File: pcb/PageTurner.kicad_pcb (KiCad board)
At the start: 2 copper layers, 32 x 20 mm, 21 parts, among them J1 AudioJack2, J2 AudioJack2, J3 USB_C_Receptacle, J5 TC2030_SWD, SW1 RST, SW2 BOOT, U1 STM32F042F6Px, U2 TPS7A0533PDBV

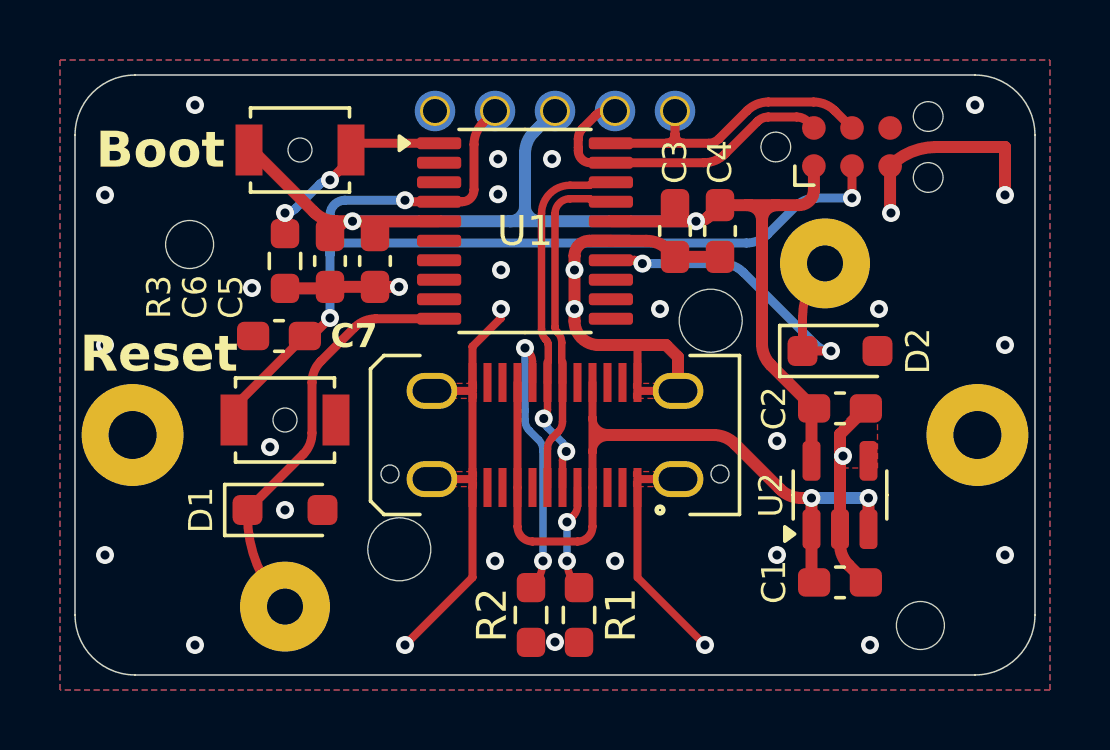
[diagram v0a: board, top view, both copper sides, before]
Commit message: Switch to a cheaper and smaller USB connector
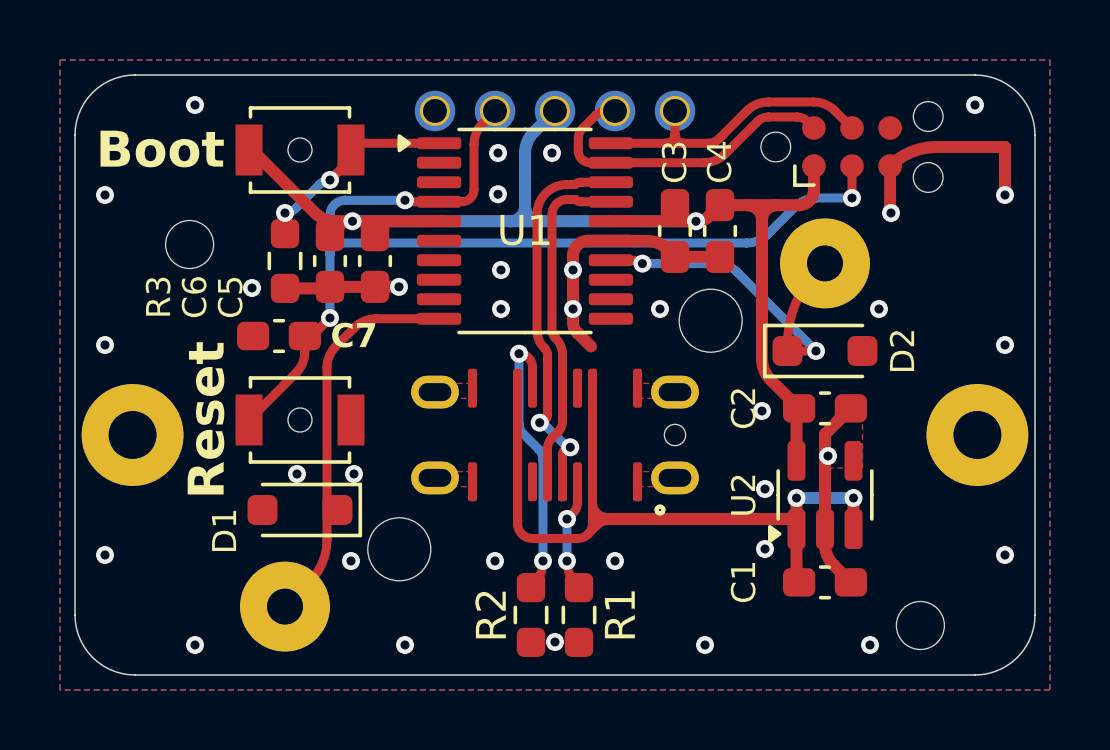
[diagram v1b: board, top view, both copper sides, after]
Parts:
- J3: footprint PageTurner:USB_C_Receptacle_JAE_DX07S024WJ3R400 -> PageTurner:USB_C_Receptacle_GCT_USB_4145
- moved C1 0.50 mm to (109.0, 104.9)
- moved C2 0.50 mm to (109.0, 99.1)
- moved D1 0.50 mm to (91.5, 102.5), turned to 180 degrees
- moved D2 0.50 mm to (109.0, 97.2)
- moved SW1 0.50 mm to (91.5, 99.5)
- moved U2 0.50 mm to (109.0, 102.0)
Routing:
- net GND: track 55.1 -> 25.7 mm, vias 32 -> 34
- net D+: track 11.8 -> 12.8 mm
- net VBUS: track 27.8 -> 26.9 mm
- net SW1: track 13.9 -> 13.0 mm

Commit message: Switch to 4 layers, add USB ESD diode
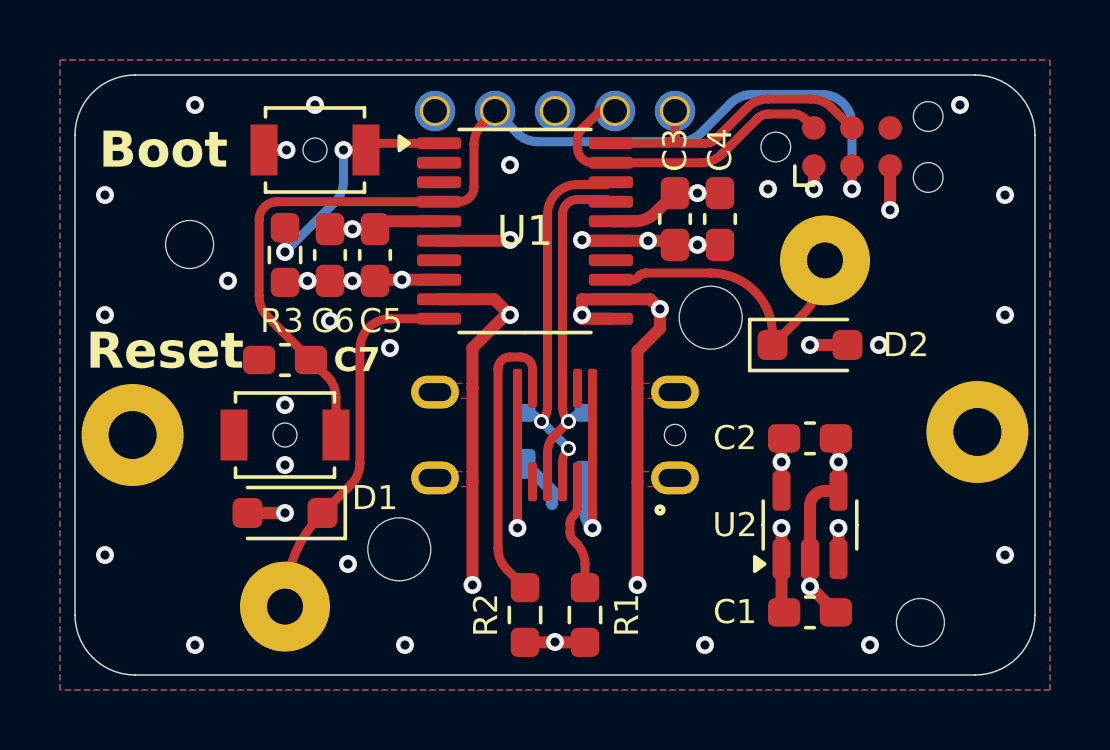
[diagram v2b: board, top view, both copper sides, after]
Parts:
- added D3: PRTR5V0U2X, Package_TO_SOT_SMD:SOT-143, B.Cu at (100.0, 100.2)
- moved C1 1.12 mm to (108.5, 105.9)
- moved C2 1.12 mm to (108.5, 100.1)
- moved U2 1.12 mm to (108.5, 103.0)
- moved C7 0.82 mm to (91.0, 97.5)
- moved SW1 0.71 mm to (91.0, 100.0), turned to 180 degrees
- moved D2 0.54 mm to (108.5, 97.0)
- moved D1 0.51 mm to (91.0, 102.6)
- moved SW2 0.50 mm to (92.0, 90.5)
- moved C3 0.40 mm to (104.0, 92.8)
- moved C4 0.40 mm to (105.5, 92.8)
- moved C5 0.20 mm to (94.0, 94.0)
- moved C6 0.20 mm to (92.5, 94.0)
- moved R1 0.20 mm to (101.0, 106.0)
- moved R2 0.20 mm to (99.0, 106.0)
- moved R3 0.20 mm to (91.0, 94.0)
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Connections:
- U1 pad 11: unconnected-(U1-PA5-Pad11) -> GND
- U1 pad 12: unconnected-(U1-PA6-Pad12) -> GND
- U1 pad 13: unconnected-(U1-PA7-Pad13) -> SW2
- U1 pad 14: SW2 -> unconnected-(U1-PB1-Pad14)
- U1 pad 6: unconnected-(U1-PA0-Pad6) -> GND
- U1 pad 7: unconnected-(U1-PA1-Pad7) -> GND
- U1 pad 8: unconnected-(U1-PA2-Pad8) -> GND
- U1 pad 9: unconnected-(U1-PA3-Pad9) -> GND
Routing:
- net +3V3: track 43.1 -> 10.6 mm, vias 2 -> 5
- net GND: track 25.7 -> 52.5 mm, vias 34 -> 40
- net BOOT0: track 5.61 -> 7.93 mm
- net SW2: track 12.3 -> 9.96 mm, vias 2 -> 0
- net RST: track 36.2 -> 34.9 mm, vias 3 -> 1
- net VBUS: track 26.9 -> 25.8 mm, vias 2 -> 4
- net SWDIO: track 10.2 -> 10.9 mm
- net SW1: track 13.0 -> 12.4 mm
- net D-: track 11.4 -> 11.7 mm, vias 0 -> 1
- net Net-(J3-CC2): track 9.58 -> 9.83 mm, vias 2 -> 0
- net Net-(J3-CC1): track 3.76 -> 3.73 mm, vias 2 -> 0
- added copper zone on In2.Cu, net +3V3
- added copper zone on In1.Cu, net GND
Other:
- copper layers 2 -> 4

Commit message: Move USB ESD to top
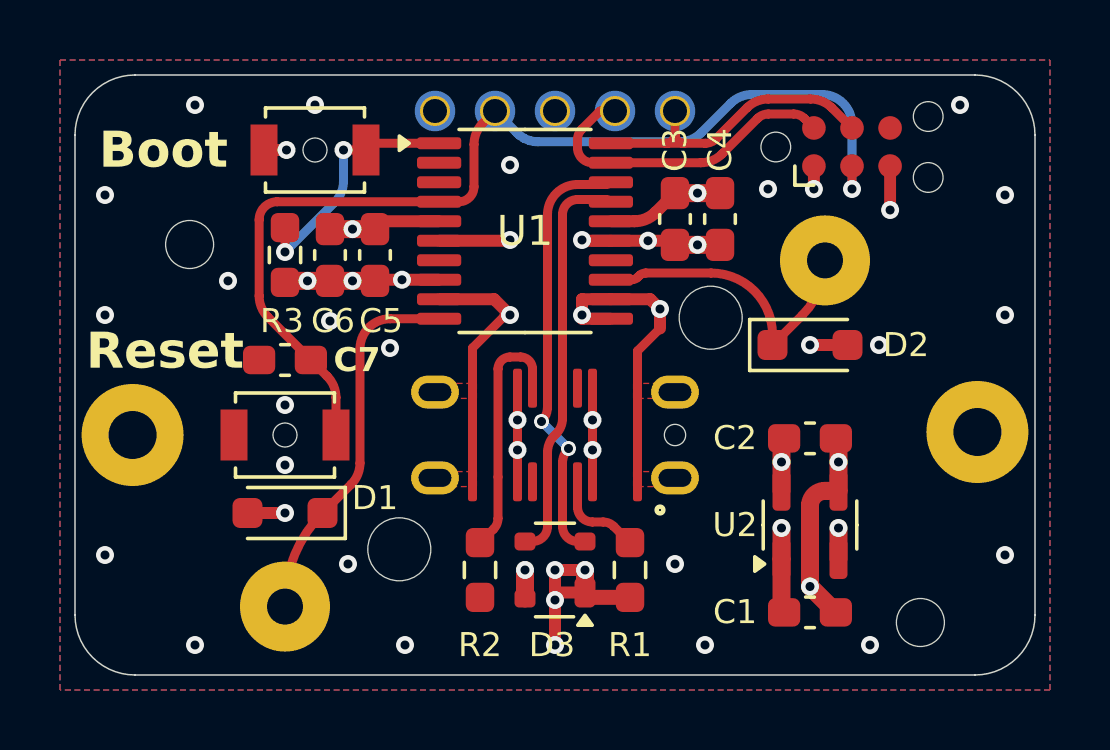
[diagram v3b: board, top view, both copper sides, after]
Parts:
- D3: moved to F.Cu
- moved D3 4.29 mm to (100.0, 104.5), turned to 180 degrees
- moved R1 2.12 mm to (102.5, 104.5)
- moved R2 2.12 mm to (97.5, 104.5)
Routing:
- net VBUS: track 25.8 -> 34.5 mm, vias 4 -> 7
- net GND: track 52.5 -> 48.7 mm, vias 40 -> 42
- net D+: track 12.7 -> 14.6 mm
- net D-: track 11.7 -> 13.4 mm, vias 1 -> 0
- net Net-(J3-CC2): track 9.83 -> 8.23 mm
- net Net-(J3-CC1): track 3.73 -> 3.12 mm

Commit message: General cleanup
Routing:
- net GND: track 48.7 -> 50.6 mm, vias 42 -> 41
- net RST: track 34.9 -> 36.6 mm
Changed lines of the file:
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@@
 		(tags "capacitor handsolder")
 		(property "Reference" "C6"
-			(at 2.2 -0.1 180)
+			(at 2.2 0 180)
 			(layer "F.SilkS")
 			(effects
@@
 		(tags "resistor handsolder")
 		(property "Reference" "R3"
-			(at 2.2 0.1 180)
+			(at 2.2 0.2 180)
 			(layer "F.SilkS")
 			(effects
@@
 		(tags "SOD-323")
 		(property "Reference" "D2"
-			(at 3.2 0 180)
+			(at 2.8 0 180)
 			(layer "F.SilkS")
 			(effects
@@
 	)
 	(segment
+		(start 100.9 97.1)
+		(end 101.7 97.1)
+		(width 0.4)
+		(layer "F.Cu")
+		(net 1)
+	)
+	(segment
 		(start 101.8625 95.475)
 		(end 100.9 95.475)
@@
 	)
 	(segment
+		(start 100.9 96)
+		(end 100.9 97.1)
+		(width 0.4)
+		(layer "F.Cu")
+		(net 1)
+	)
+	(segment
 		(start 100.925 93.525)
 		(end 100.9 93.5)
@@
 	)
 	(via
-		(at 92.5 96.2)
+		(at 115 96)
 		(size 0.6)
 		(drill 0.3)
@@
 	)
 	(via
-		(at 115 96)
+		(at 98.5 96)
 		(size 0.6)
 		(drill 0.3)
@@
 	)
 	(via
-		(at 98.5 96)
+		(at 103.1 93.525)
 		(size 0.6)
 		(drill 0.3)
 		(layers "F.Cu" "B.Cu")
-		(free yes)
 		(net 1)
 	)
 	(via
-		(at 103.1 93.525)
+		(at 115 92)
 		(size 0.6)
 		(drill 0.3)
 		(layers "F.Cu" "B.Cu")
+		(free yes)
 		(net 1)
 	)
 	(via
-		(at 115 92)
+		(at 110.6 101.8625)
 		(size 0.6)
 		(drill 0.3)
@@
 	)
 	(via
-		(at 105 107)
+		(at 106 107)
 		(size 0.6)
 		(drill 0.3)
@@
 	)
 	(via
-		(at 94.5 97.1)
-		(size 0.6)
-		(drill 0.3)
-		(layers "F.Cu" "B.Cu")
-		(free yes)
-		(net 1)
-	)
-	(via
 		(at 100 104.5)
 		(size 0.6)
@@
 	)
 	(via
-		(at 89.1 94.8625)
+		(at 89.1 96)
 		(size 0.6)
 		(drill 0.3)
@@
 	)
 	(via
-		(at 95 107)
+		(at 94 107)
 		(size 0.6)
 		(drill 0.3)
@@
 	)
 	(via
-		(at 107.1 91.8)
+		(at 107 91.6)
 		(size 0.6)
 		(drill 0.3)
@@
 	)
 	(via
-		(at 110.8 97)
+		(at 111 96)
 		(size 0.6)
 		(drill 0.3)
@@
 	)
 	(via
-		(at 93.1 104.3)
+		(at 89.1 92)
 		(size 0.6)
 		(drill 0.3)
@@
 	)
 	(segment
-		(start 90.7375 92.225)
-		(end 96.1375 92.225)
+		(start 92.7 100)
+		(end 92.7 97.5)
 		(width 0.3)
 		(layer "F.Cu")
@@
 	)
 	(segment
-		(start 91.8625 97.5)
-		(end 90.430393 96.067893)
+		(start 97.3 91.725)
+		(end 97.3 90.314214)
 		(width 0.3)
 		(layer "F.Cu")
@@
 	)
 	(segment
-		(start 92.407107 98.044607)
-		(end 91.8625 97.5)
+		(start 91.8625 97.5)
+		(end 92.7 97.5)
 		(width 0.3)
 		(layer "F.Cu")
@@
 	)
 	(segment
-		(start 90.1375 95.360786)
-		(end 90.1375 92.825)
+		(start 96.1375 92.225)
+		(end 90.7875 92.225)
 		(width 0.3)
 		(layer "F.Cu")
@@
 	)
 	(segment
-		(start 97.3 91.725)
-		(end 97.3 90.314214)
+		(start 90.7875 95.8)
+		(end 91.7 95.8)
 		(width 0.3)
 		(layer "F.Cu")
@@
 	)
 	(segment
-		(start 92.7 100)
-		(end 92.7 98.751714)
+		(start 97.592893 89.607107)
+		(end 98 89.2)
 		(width 0.3)
 		(layer "F.Cu")
@@
 	)
 	(segment
-		(start 97.592893 89.607107)
-		(end 98 89.2)
+		(start 90.1375 92.875)
+		(end 90.1375 95.15)
 		(width 0.3)
 		(layer "F.Cu")
@@
 	)
 	(segment
+		(start 92.7 96.8)
+		(end 92.7 97.5)
+		(width 0.3)
+		(layer "F.Cu")
+		(net 12)
+	)
+	(segment
 		(start 109.9 91.035)
 		(end 109.9 91.8)
@@
 	)
 	(arc
-		(start 90.430393 96.067893)
-		(mid 90.21362 95.74347)
-		(end 90.1375 95.360786)
+		(start 90.7875 95.8)
+		(mid 90.327881 95.609619)
+		(end 90.1375 95.15)
 		(width 0.3)
 		(layer "F.Cu")
@@
 	)
 	(arc
-		(start 90.7375 92.225)
-		(mid 90.313236 92.400736)
-		(end 90.1375 92.825)
+		(start 91.7 95.8)
+		(mid 92.407107 96.092893)
+		(end 92.7 96.8)
 		(width 0.3)
 		(layer "F.Cu")
@@
 	)
 	(arc
-		(start 92.407107 98.044607)
-		(mid 92.62388 98.36903)
-		(end 92.7 98.751714)
+		(start 90.1375 92.875)
+		(mid 90.327881 92.415381)
+		(end 90.7875 92.225)
 		(width 0.3)
 		(layer "F.Cu")
@@
 	)
 	(segment
-		(start 101.5 89.2)
-		(end 102 89.2)
-		(width 0.3)
-		(layer "F.Cu")
-		(net 15)
-	)
-	(segment
 		(start 100.896447 89.803553)
-		(end 101.5 89.2)
+		(end 101.146446 89.553554)
 		(width 0.3)
 		(layer "F.Cu")
@@
 		(width 0.3)
 		(layer "F.Cu")
+		(net 15)
+	)
+	(arc
+		(start 101.146446 89.553554)
+		(mid 101.53806 89.291886)
+		(end 102 89.2)
+		(width 0.3)
+		(layer "F.Cu")

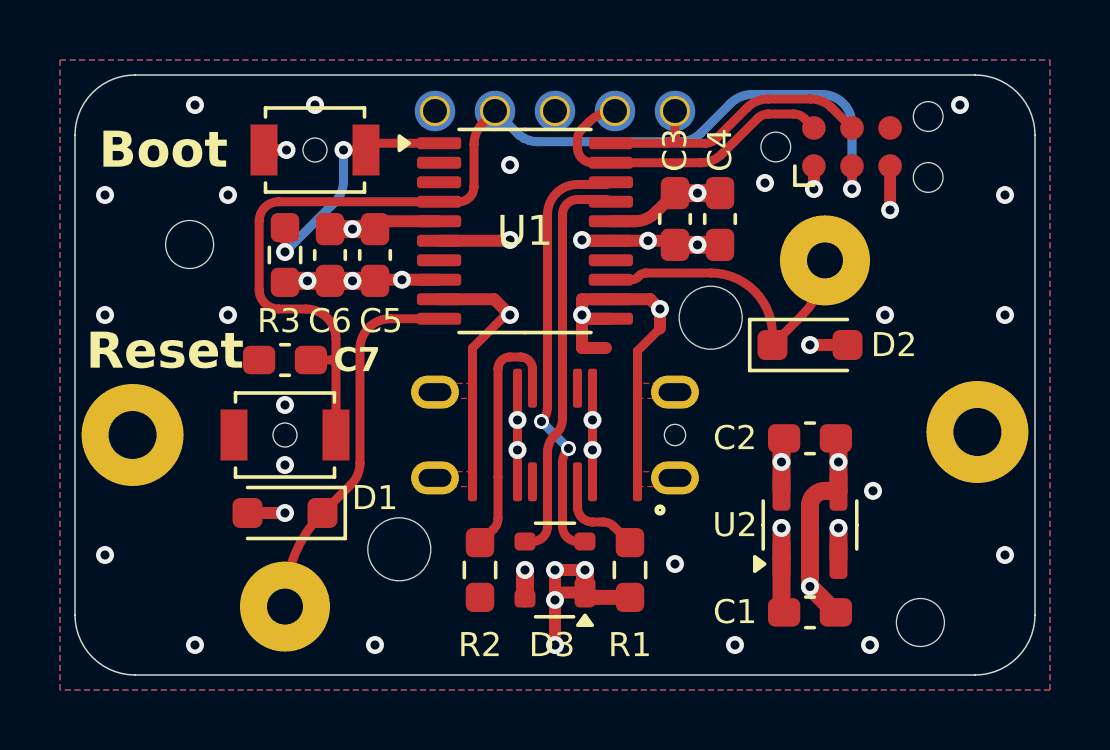
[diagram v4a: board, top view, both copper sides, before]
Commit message: Disconnect GPIOs from GND
GPIOs are supposed to power up in floating input mode, so I tied some of
them to GND for easier routing. For some reason the input voltage sagged
to ~0.6 V until I disconnected these pins from the PCB though. I'm not
sure if this was the cause or I just messed up soldering something, but
disconnecting these just to be safe.
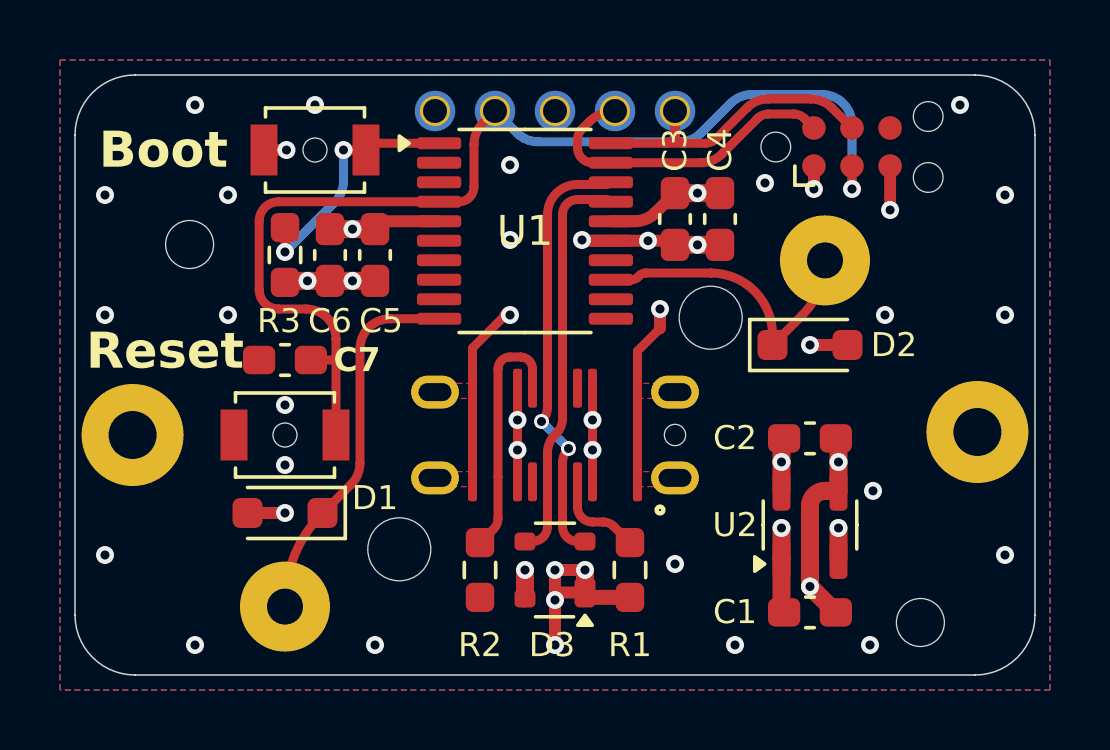
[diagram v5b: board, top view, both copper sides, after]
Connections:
- U1 pad 11: GND -> unconnected-(U1-PA5-Pad11)
- U1 pad 12: GND -> unconnected-(U1-PA6-Pad12)
- U1 pad 6: GND -> unconnected-(U1-PA0-Pad6)
- U1 pad 7: GND -> unconnected-(U1-PA1-Pad7)
- U1 pad 8: GND -> unconnected-(U1-PA2-Pad8)
- U1 pad 9: GND -> unconnected-(U1-PA3-Pad9)
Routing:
- net GND: track 50.6 -> 37.3 mm, vias 41 -> 39
